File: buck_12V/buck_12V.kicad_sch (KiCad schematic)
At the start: 8 parts, among them U1101 ST1S10PHR

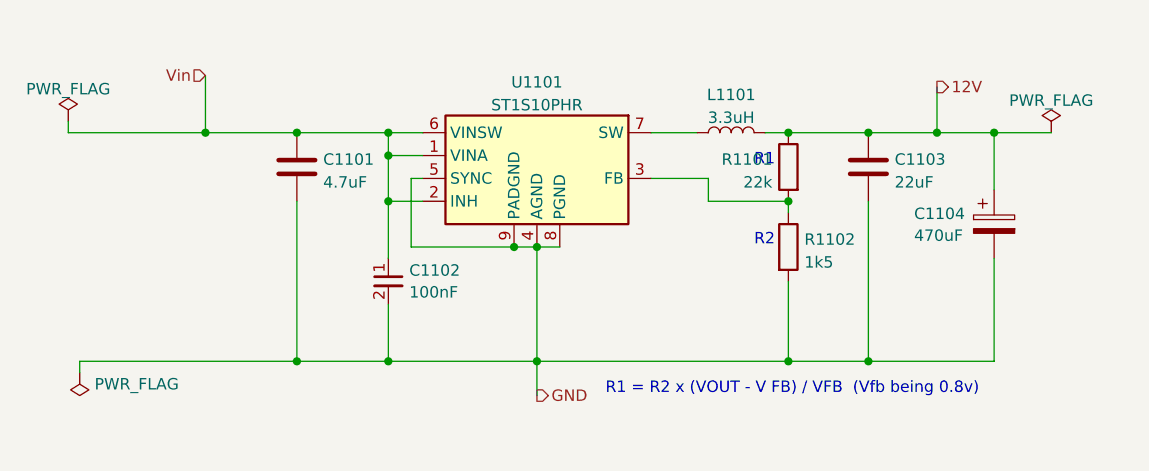
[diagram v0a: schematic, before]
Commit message: also updated 12v buck converter with power symbols
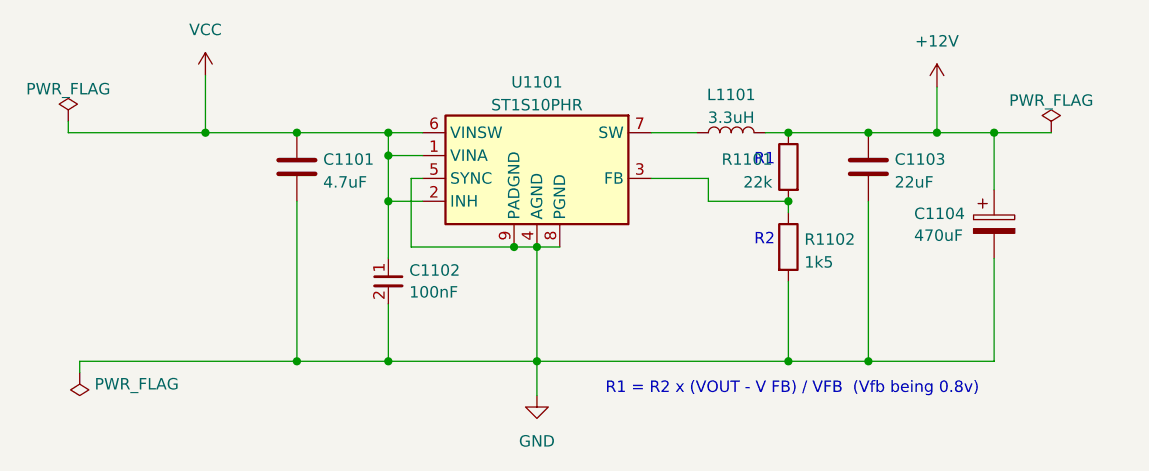
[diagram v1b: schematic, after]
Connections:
- net 12V renamed +12V
- net Vin renamed VCC
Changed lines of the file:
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@@
     (effects (font (size 1.27 1.27)) (justify left bottom))
-  )
-  (hierarchical_label "12V" (shape output) (at 189.23 74.93 0) (fields_autoplaced)
-    (effects (font (size 1.27 1.27)) (justify left))
-  )
-  (hierarchical_label "GND" (shape output) (at 144.78 109.22 0) (fields_autoplaced)
-    (effects (font (size 1.27 1.27)) (justify left))
-  )
-  (hierarchical_label "Vin" (shape input) (at 107.95 73.66 180) (fields_autoplaced)
-    (effects (font (size 1.27 1.27)) (justify right))
   )
   (symbol (lib_id "power:PWR_FLAG") (at 201.93 80.01 0) (unit 1)
@@
         (path "/e63e39d7-6ac0-4ffd-8aa3-1841a4541b55/86e0260b-4a03-44ef-825c-afa574dfce06"
           (reference "#FLG0502") (unit 1)
+        )
+      )
+    )
+  )
+  (symbol (lib_id "power:VCC") (at 107.95 73.66 0) (unit 1)
+    (in_bom yes) (on_board yes) (dnp no) (fields_autoplaced)
+    (property "Reference" "#PWR01101" (at 107.95 77.47 0)
+      (effects (font (size 1.27 1.27)) hide)
+    )
+    (property "Value" "VCC" (at 107.95 68.58 0)
+      (effects (font (size 1.27 1.27)))
+    )
+    (property "Footprint" "" (at 107.95 73.66 0)
+      (effects (font (size 1.27 1.27)) hide)
+    )
+    (property "Datasheet" "" (at 107.95 73.66 0)
+      (effects (font (size 1.27 1.27)) hide)
+    )
+    (pin "1")
+    (instances
+      (project "buck_12V"
+        (path "/4ad43733-e20a-49f3-807e-18598232469f"
+          (reference "#PWR01101") (unit 1)
         )
       )
@@
     )
   )
+  (symbol (lib_id "power:+12V") (at 189.23 74.93 0) (unit 1)
+    (in_bom yes) (on_board yes) (dnp no) (fields_autoplaced)
+    (property "Reference" "#PWR01102" (at 189.23 78.74 0)
+      (effects (font (size 1.27 1.27)) hide)
+    )
+    (property "Value" "+12V" (at 189.23 69.85 0)
+      (effects (font (size 1.27 1.27)))
+    )
+    (property "Footprint" "" (at 189.23 74.93 0)
+      (effects (font (size 1.27 1.27)) hide)
+    )
+    (property "Datasheet" "" (at 189.23 74.93 0)
+      (effects (font (size 1.27 1.27)) hide)
+    )
+    (pin "1")
+    (instances
+      (project "buck_12V"
+        (path "/4ad43733-e20a-49f3-807e-18598232469f"
+          (reference "#PWR01102") (unit 1)
+        )
+      )
+    )
+  )
   (symbol (lib_id "Device:C") (at 118.11 83.82 0) (unit 1)
     (in_bom yes) (on_board yes) (dnp no) (fields_autoplaced)
@@
         )
       )
+    )
+  )
+  (symbol (lib_id "power:GND") (at 144.78 109.22 0) (unit 1)
+    (in_bom yes) (on_board yes) (dnp no) (fields_autoplaced)
+    (property "Reference" "#PWR01103" (at 144.78 115.57 0)
+      (effects (font (size 1.27 1.27)) hide)
+    )
+    (property "Value" "GND" (at 144.78 114.3 0)
+      (effects (font (size 1.27 1.27)))
+    )
+    (property "Footprint" "" (at 144.78 109.22 0)
+      (effects (font (size 1.27 1.27)) hide)
+    )
+    (property "Datasheet" "" (at 144.78 109.22 0)
+      (effects (font (size 1.27 1.27)) hide)
+    )
+    (pin "1")
+    (instances
+      (project "buck_12V"
+        (path "/4ad43733-e20a-49f3-807e-18598232469f"
+          (reference "#PWR01103") (unit 1)
+        )
+      )
